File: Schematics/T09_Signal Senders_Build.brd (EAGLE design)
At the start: 88.6 x 64.8 mm, 40 parts, among them IC1 7805TV, IC2 7805TV, IC3 ATMEGA328, SW1 UNIT_ID, X1 , Y2 16MHz

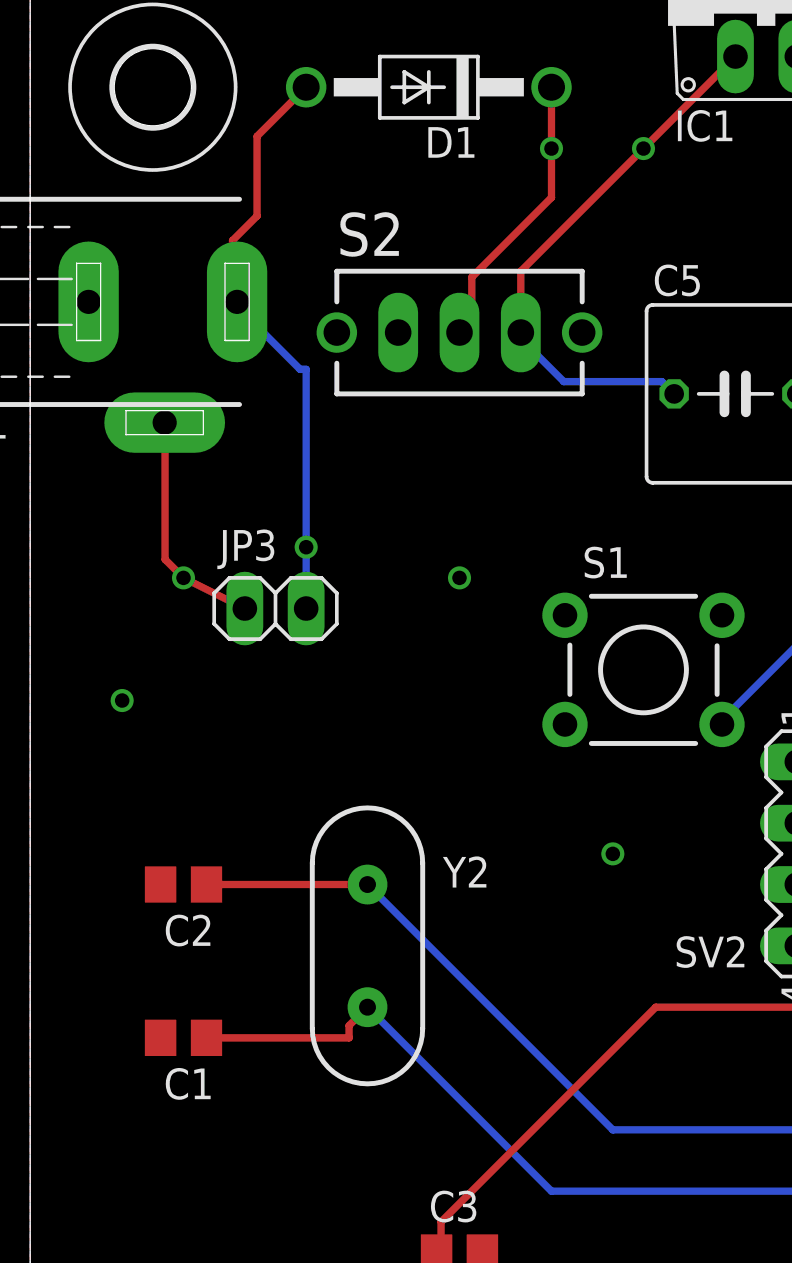
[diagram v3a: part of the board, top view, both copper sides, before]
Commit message: Minor changes to traces.
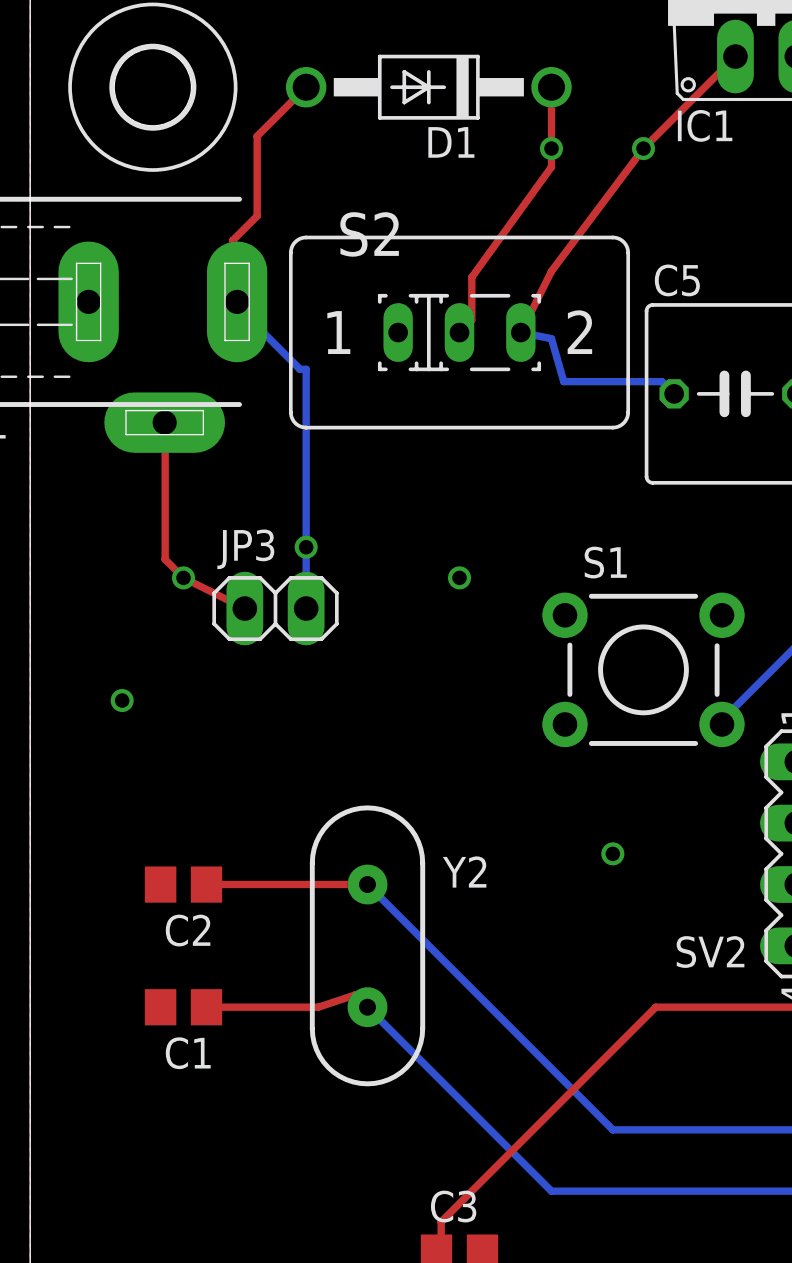
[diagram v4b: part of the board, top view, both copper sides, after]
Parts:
- S2: device switch:TL3XYO -> switch:M251
- moved C1 1.27 mm to (6.35, 21.6)
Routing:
- net N$2: track 33.5 -> 33.0 mm
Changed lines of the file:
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@@
 <attribute name="NAME" x="74.93" y="60.96" size="1.27" layer="25"/>
 </element>
-<element name="C1" library="rcl" package="C0805" value="22pF" x="6.35" y="20.32" smashed="yes" rot="R180">
-<attribute name="NAME" x="7.62" y="19.05" size="1.27" layer="25" rot="R180"/>
+<element name="C1" library="rcl" package="C0805" value="22pF" x="6.35" y="21.59" smashed="yes" rot="R180">
+<attribute name="NAME" x="7.62" y="20.32" size="1.27" layer="25" rot="R180"/>
 </element>
 <element name="JP1" library="pinhead" package="2X04" value=" RF" x="83.82" y="17.78" smashed="yes" rot="R90">
@@
 <attribute name="NAME" x="69.342" y="39.116" size="1.27" layer="25" ratio="10" rot="R180"/>
 </element>
-<element name="S2" library="switch" package="TL3XYO" value="POWER" x="17.78" y="49.53" smashed="yes">
+<element name="S2" library="switch" package="M251" value="POWER" x="17.78" y="49.53" smashed="yes">
 <attribute name="NAME" x="12.7" y="52.705" size="1.778" layer="25"/>
 <attribute name="VALUE" x="12.7" y="44.45" size="1.778" layer="27"/>
@@
 <contactref element="C1" pad="1"/>
 <contactref element="Y2" pad="1"/>
-<wire x1="13.208" y1="20.32" x2="7.3" y2="20.32" width="0.3048" layer="1"/>
-<wire x1="13.208" y1="20.828" x2="13.208" y2="20.32" width="0.3048" layer="1"/>
-<wire x1="13.97" y1="21.59" x2="13.208" y2="20.828" width="0.3048" layer="1"/>
+<wire x1="11.938" y1="21.59" x2="7.3" y2="21.59" width="0.3048" layer="1"/>
+<wire x1="13.462" y1="22.098" x2="11.938" y2="21.59" width="0.3048" layer="1"/>
+<wire x1="13.97" y1="21.59" x2="13.462" y2="22.098" width="0.3048" layer="1"/>
 <wire x1="21.59" y1="13.97" x2="36.83" y2="13.97" width="0.3048" layer="16"/>
 <wire x1="13.97" y1="21.59" x2="21.59" y2="13.97" width="0.3048" layer="16"/>
@@
 <wire x1="26.162" y1="47.498" x2="26.67" y2="46.99" width="0.3048" layer="16"/>
 <wire x1="22.098" y1="47.498" x2="26.162" y2="47.498" width="0.3048" layer="16"/>
-<wire x1="20.32" y1="49.276" x2="22.098" y2="47.498" width="0.3048" layer="16"/>
-<wire x1="20.32" y1="49.53" x2="20.32" y2="49.276" width="0.3048" layer="16"/>
-<wire x1="20.32" y1="52.07" x2="25.4" y2="57.15" width="0.3048" layer="1"/>
+<wire x1="21.59" y1="49.276" x2="22.098" y2="47.498" width="0.3048" layer="16"/>
+<wire x1="20.32" y1="49.53" x2="21.59" y2="49.276" width="0.3048" layer="16"/>
+<wire x1="21.59" y1="52.07" x2="25.4" y2="57.15" width="0.3048" layer="1"/>
 <wire x1="25.4" y1="57.15" x2="29.21" y2="60.96" width="0.3048" layer="1"/>
-<wire x1="20.32" y1="49.53" x2="20.32" y2="52.07" width="0.3048" layer="1"/>
+<wire x1="20.32" y1="49.53" x2="21.59" y2="52.07" width="0.3048" layer="1"/>
 <via x="25.4" y="57.15" extent="1-16" drill="0.6"/>
 </signal>
@@
 <wire x1="18.288" y1="50.038" x2="17.78" y2="49.53" width="0.3048" layer="1"/>
 <wire x1="18.288" y1="51.816" x2="18.288" y2="50.038" width="0.3048" layer="1"/>
-<wire x1="21.59" y1="55.118" x2="18.288" y2="51.816" width="0.3048" layer="1"/>
+<wire x1="21.59" y1="56.388" x2="18.288" y2="51.816" width="0.3048" layer="1"/>
 <wire x1="21.59" y1="59.69" x2="21.59" y2="57.15" width="0.3048" layer="1"/>
-<wire x1="21.59" y1="57.15" x2="21.59" y2="55.118" width="0.3048" layer="1"/>
+<wire x1="21.59" y1="57.15" x2="21.59" y2="56.388" width="0.3048" layer="1"/>
 <via x="21.59" y="57.15" extent="1-16" drill="0.6"/>
 </signal>

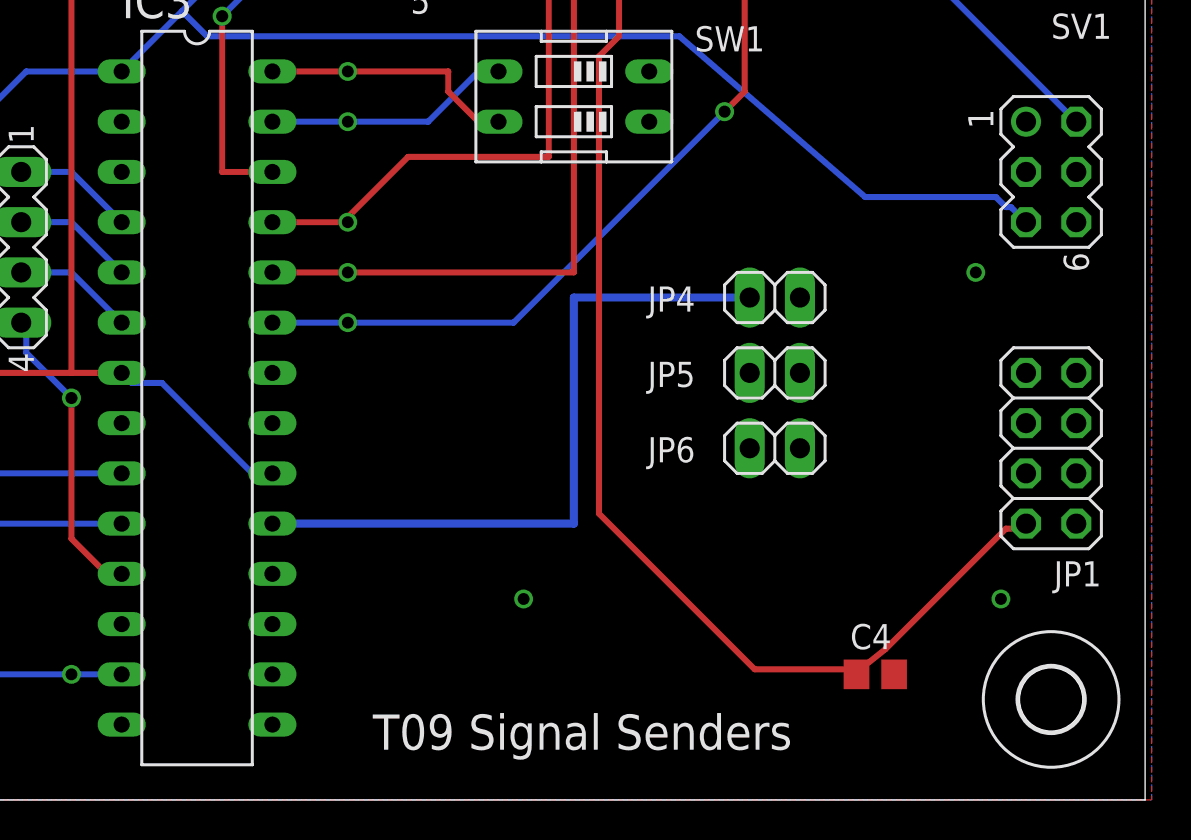
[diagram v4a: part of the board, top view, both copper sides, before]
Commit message: routed traces to PCB
last commit didn't seem to work
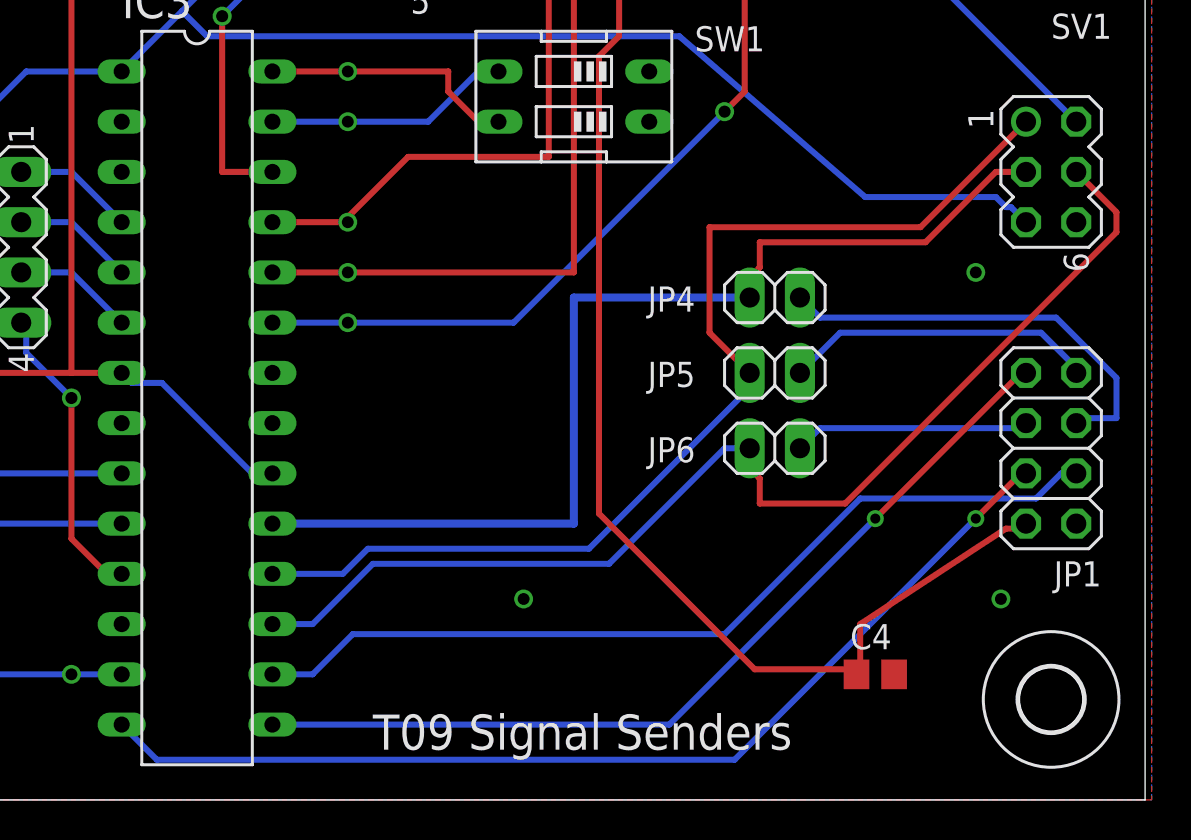
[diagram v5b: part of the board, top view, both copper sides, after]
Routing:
- net N$32: track 0.00 -> 58.4 mm
- net N$31: track 0.00 -> 55.2 mm
- net N$34: track 0.00 -> 52.5 mm, vias 0 -> 1
- net N$35: track 0.00 -> 45.5 mm, vias 0 -> 1
- net N$36: track 0.00 -> 44.8 mm
- net N$39: track 0.00 -> 21.9 mm
- net N$33: track 35.6 -> 53.5 mm
- net N$38: track 0.00 -> 15.8 mm
- net N$37: track 0.00 -> 12.0 mm
- net +3V3: track 77.3 -> 78.1 mm
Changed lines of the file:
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@@
 <?xml version="1.0" encoding="utf-8"?>
 <!DOCTYPE eagle SYSTEM "eagle.dtd">
-<eagle version="6.3">
+<eagle version="6.5.0">
 <drawing>
 <settings>
@@
 <wire x1="58.42" y1="60.96" x2="58.42" y2="59.69" width="0.3048" layer="1"/>
 <wire x1="61.722" y1="54.61" x2="61.91" y2="54.61" width="0.3048" layer="1"/>
-<wire x1="75.438" y1="7.62" x2="74.168" y2="6.604" width="0.3048" layer="1"/>
+<wire x1="74.168" y1="8.89" x2="74.168" y2="6.604" width="0.3048" layer="1"/>
 <wire x1="74.168" y1="6.604" x2="74.168" y2="6.35" width="0.3048" layer="1"/>
-<wire x1="81.534" y1="13.716" x2="75.438" y2="7.62" width="0.3048" layer="1"/>
+<wire x1="81.534" y1="13.716" x2="74.168" y2="8.89" width="0.3048" layer="1"/>
 <wire x1="82.55" y1="13.716" x2="81.534" y2="13.716" width="0.3048" layer="1"/>
 <wire x1="82.55" y1="13.97" x2="82.55" y2="13.716" width="0.3048" layer="1"/>
@@
 <contactref element="SV1" pad="3"/>
 <contactref element="JP4" pad="1"/>
-<wire x1="68.58" y1="25.4" x2="82.55" y2="31.75" width="0" layer="19" extent="1-1"/>
-<wire x1="44.45" y1="13.97" x2="68.58" y2="25.4" width="0" layer="19" extent="1-1"/>
 <wire x1="44.45" y1="13.97" x2="59.69" y2="13.97" width="0.4064" layer="16"/>
 <wire x1="59.69" y1="13.97" x2="59.69" y2="25.4" width="0.4064" layer="16"/>
 <wire x1="59.69" y1="25.4" x2="68.58" y2="25.4" width="0.4064" layer="16"/>
+<wire x1="81.026" y1="31.75" x2="82.55" y2="31.75" width="0.3048" layer="1"/>
+<wire x1="77.47" y1="28.194" x2="81.026" y2="31.75" width="0.3048" layer="1"/>
+<wire x1="69.088" y1="28.194" x2="77.47" y2="28.194" width="0.3048" layer="1"/>
+<wire x1="69.088" y1="26.924" x2="69.088" y2="28.194" width="0.3048" layer="1"/>
+<wire x1="68.58" y1="26.416" x2="69.088" y2="26.924" width="0.3048" layer="1"/>
+<wire x1="68.58" y1="25.4" x2="68.58" y2="26.416" width="0.3048" layer="1"/>
 </signal>
 <signal name="N$34">
 <contactref element="JP1" pad="4"/>
 <contactref element="IC3" pad="14"/>
-<wire x1="36.83" y1="3.81" x2="82.55" y2="16.51" width="0" layer="19" extent="1-1"/>
+<wire x1="38.608" y1="2.032" x2="36.83" y2="3.81" width="0.3048" layer="16"/>
+<wire x1="67.818" y1="2.032" x2="38.608" y2="2.032" width="0.3048" layer="16"/>
+<wire x1="80.01" y1="14.224" x2="67.818" y2="2.032" width="0.3048" layer="16"/>
+<wire x1="82.296" y1="16.51" x2="80.01" y2="14.224" width="0.3048" layer="1"/>
+<wire x1="82.55" y1="16.51" x2="82.296" y2="16.51" width="0.3048" layer="1"/>
+<via x="80.01" y="14.224" extent="1-16" drill="0.508"/>
 </signal>
 <signal name="N$35">
 <contactref element="JP1" pad="8"/>
 <contactref element="IC3" pad="15"/>
-<wire x1="44.45" y1="3.81" x2="82.55" y2="21.59" width="0" layer="19" extent="1-1"/>
+<wire x1="64.516" y1="3.81" x2="44.45" y2="3.81" width="0.3048" layer="16"/>
+<wire x1="74.93" y1="14.224" x2="64.516" y2="3.81" width="0.3048" layer="16"/>
+<wire x1="82.296" y1="21.59" x2="74.93" y2="14.224" width="0.3048" layer="1"/>
+<wire x1="82.55" y1="21.59" x2="82.296" y2="21.59" width="0.3048" layer="1"/>
+<via x="74.93" y="14.224" extent="1-16" drill="0.508"/>
 </signal>
 <signal name="N$36">
 <contactref element="IC3" pad="16"/>
 <contactref element="JP1" pad="3"/>
-<wire x1="44.45" y1="6.35" x2="85.09" y2="16.51" width="0" layer="19" extent="1-1"/>
+<wire x1="46.482" y1="6.35" x2="44.45" y2="6.35" width="0.3048" layer="16"/>
+<wire x1="48.514" y1="8.382" x2="46.482" y2="6.35" width="0.3048" layer="16"/>
+<wire x1="67.31" y1="8.382" x2="48.514" y2="8.382" width="0.3048" layer="16"/>
+<wire x1="74.168" y1="15.24" x2="67.31" y2="8.382" width="0.3048" layer="16"/>
+<wire x1="83.058" y1="15.24" x2="74.168" y2="15.24" width="0.3048" layer="16"/>
+<wire x1="84.328" y1="16.51" x2="83.058" y2="15.24" width="0.3048" layer="16"/>
+<wire x1="85.09" y1="16.51" x2="84.328" y2="16.51" width="0.3048" layer="16"/>
 </signal>
 <signal name="N$37">
 <contactref element="JP6" pad="2"/>
 <contactref element="JP1" pad="6"/>
-<wire x1="71.12" y1="17.78" x2="82.55" y2="19.05" width="0" layer="19" extent="1-1"/>
+<wire x1="72.136" y1="18.796" x2="71.12" y2="17.78" width="0.3048" layer="16"/>
+<wire x1="82.296" y1="18.796" x2="72.136" y2="18.796" width="0.3048" layer="16"/>
+<wire x1="82.55" y1="19.05" x2="82.296" y2="18.796" width="0.3048" layer="16"/>
 </signal>
 <signal name="N$38">
 <contactref element="JP5" pad="2"/>
 <contactref element="JP1" pad="7"/>
-<wire x1="71.12" y1="21.59" x2="85.09" y2="21.59" width="0" layer="19" extent="1-1"/>
+<wire x1="73.152" y1="23.622" x2="71.12" y2="21.59" width="0.3048" layer="16"/>
+<wire x1="83.312" y1="23.622" x2="73.152" y2="23.622" width="0.3048" layer="16"/>
+<wire x1="85.09" y1="21.844" x2="83.312" y2="23.622" width="0.3048" layer="16"/>
+<wire x1="85.09" y1="21.59" x2="85.09" y2="21.844" width="0.3048" layer="16"/>
 </signal>
 <signal name="N$39">
 <contactref element="JP4" pad="2"/>
 <contactref element="JP1" pad="5"/>
-<wire x1="71.12" y1="25.4" x2="85.09" y2="19.05" width="0" layer="19" extent="1-1"/>
+<wire x1="72.136" y1="24.384" x2="71.12" y2="25.4" width="0.3048" layer="16"/>
+<wire x1="84.074" y1="24.384" x2="72.136" y2="24.384" width="0.3048" layer="16"/>
+<wire x1="87.122" y1="21.336" x2="84.074" y2="24.384" width="0.3048" layer="16"/>
+<wire x1="87.122" y1="19.304" x2="87.122" y2="21.336" width="0.3048" layer="16"/>
+<wire x1="85.344" y1="19.304" x2="87.122" y2="19.304" width="0.3048" layer="16"/>
+<wire x1="85.09" y1="19.05" x2="85.344" y2="19.304" width="0.3048" layer="16"/>
 </signal>
 <signal name="N$31">
@@
 <contactref element="SV1" pad="1"/>
 <contactref element="JP5" pad="1"/>
-<wire x1="68.58" y1="21.59" x2="82.55" y2="34.29" width="0" layer="19" extent="1-1"/>
-<wire x1="44.45" y1="11.43" x2="68.58" y2="21.59" width="0" layer="19" extent="1-1"/>
+<wire x1="48.006" y1="11.43" x2="44.45" y2="11.43" width="0.3048" layer="16"/>
+<wire x1="49.276" y1="12.7" x2="48.006" y2="11.43" width="0.3048" layer="16"/>
+<wire x1="60.452" y1="12.7" x2="49.276" y2="12.7" width="0.3048" layer="16"/>
+<wire x1="68.58" y1="20.828" x2="60.452" y2="12.7" width="0.3048" layer="16"/>
+<wire x1="68.58" y1="21.59" x2="68.58" y2="20.828" width="0.3048" layer="16"/>
+<wire x1="77.216" y1="28.956" x2="82.55" y2="34.29" width="0.3048" layer="1"/>
+<wire x1="66.548" y1="28.956" x2="77.216" y2="28.956" width="0.3048" layer="1"/>
+<wire x1="66.548" y1="23.622" x2="66.548" y2="28.956" width="0.3048" layer="1"/>
+<wire x1="68.58" y1="21.59" x2="66.548" y2="23.622" width="0.3048" layer="1"/>
 </signal>
 <signal name="N$32">
@@
 <contactref element="SV1" pad="4"/>
 <contactref element="JP6" pad="1"/>
-<wire x1="68.58" y1="17.78" x2="85.09" y2="31.75" width="0" layer="19" extent="1-1"/>
-<wire x1="44.45" y1="8.89" x2="68.58" y2="17.78" width="0" layer="19" extent="1-1"/>
+<wire x1="46.482" y1="8.89" x2="44.45" y2="8.89" width="0.3048" layer="16"/>
+<wire x1="49.53" y1="11.938" x2="46.482" y2="8.89" width="0.3048" layer="16"/>
+<wire x1="61.468" y1="11.938" x2="49.53" y2="11.938" width="0.3048" layer="16"/>
+<wire x1="67.31" y1="17.78" x2="61.468" y2="11.938" width="0.3048" layer="16"/>
+<wire x1="68.58" y1="17.78" x2="67.31" y2="17.78" width="0.3048" layer="16"/>
+<wire x1="87.122" y1="29.718" x2="85.09" y2="31.75" width="0.3048" layer="1"/>
+<wire x1="87.122" y1="28.702" x2="87.122" y2="29.718" width="0.3048" layer="1"/>
+<wire x1="73.406" y1="14.986" x2="87.122" y2="28.702" width="0.3048" layer="1"/>
+<wire x1="69.088" y1="14.986" x2="73.406" y2="14.986" width="0.3048" layer="1"/>
+<wire x1="69.088" y1="16.256" x2="69.088" y2="14.986" width="0.3048" layer="1"/>
+<wire x1="68.58" y1="16.764" x2="69.088" y2="16.256" width="0.3048" layer="1"/>
+<wire x1="68.58" y1="17.78" x2="68.58" y2="16.764" width="0.3048" layer="1"/>
 </signal>
 </signals>
